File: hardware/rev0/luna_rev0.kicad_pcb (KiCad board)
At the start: 4 copper layers, 48.9 x 50 mm, 132 parts, among them IC1 ECP5-BGA256, J1 USB_B_Micro, J2 USB_B_Micro, J3 USB_A, J4 USB_B_Micro, J5 Conn_ARM_JTAG_SWD_10, J6 Conn_ARM_JTAG_SWD_10, J7 Conn_02x02_Counter_Clockwise, J8 Conn_Coaxial, J9 Conn_Coaxial, SW1 BTN_RECOVERY, SW2 BTN_DFU, SW3 BTN_RESET, U1 AP22814-SOT, U10 S27KS0641, U11 USB3343, U12 AP22814-SOT, U2 MIC5504-1.8YM5, U3 MIC5219-3.3YM5, U4 TCR2EF11, U5 MIC5504-2.5YM5, U6 ATSAMD21G18A-AUT, U7 W25Q32JVSS, U8 USB3343, U9 USB3343, Y1 DSC60xx

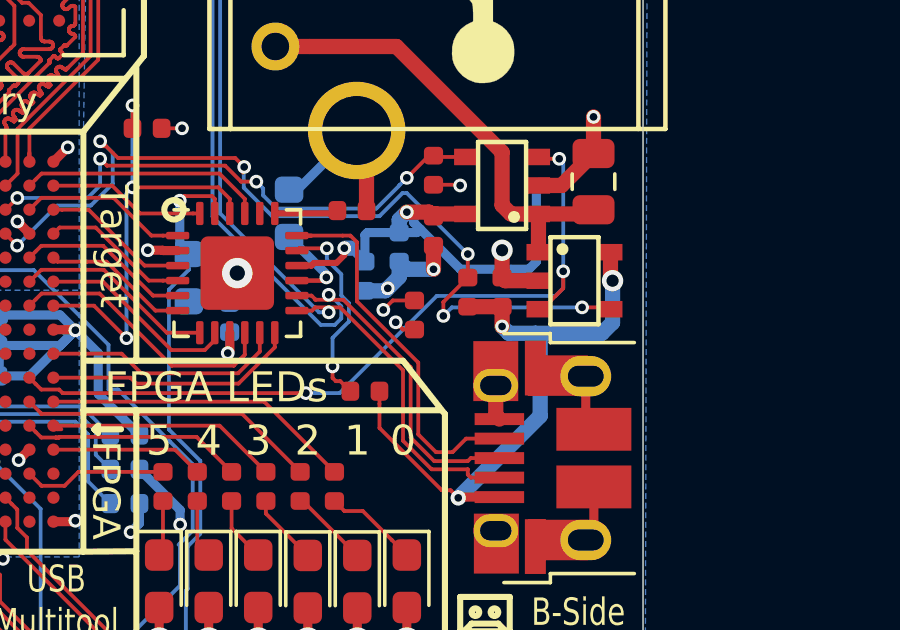
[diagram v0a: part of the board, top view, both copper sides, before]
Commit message: hardware: correct R3 footprint
fix #11
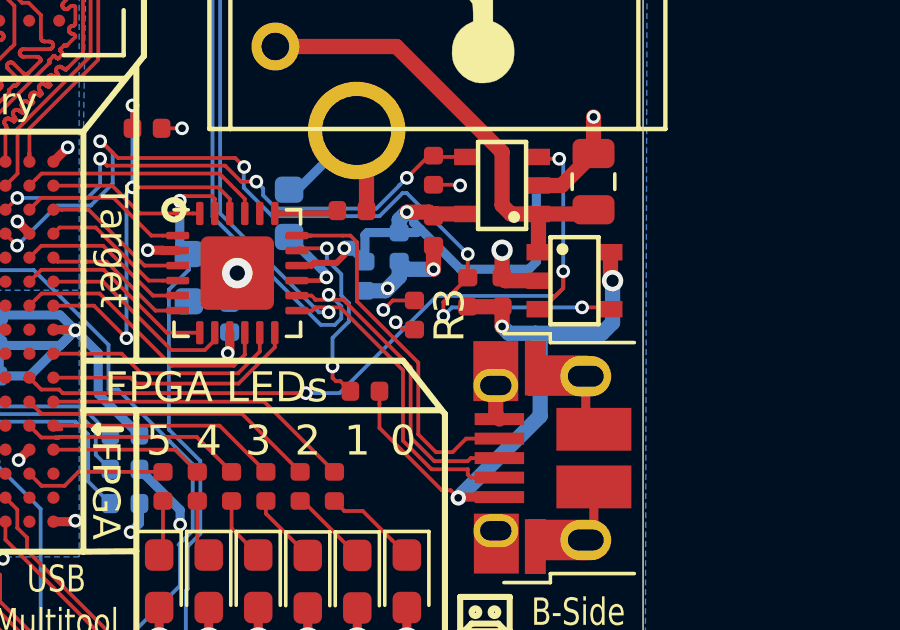
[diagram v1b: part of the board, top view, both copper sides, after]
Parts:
- R12, R13, R14: value 10k -> 10K
- R17, R19, R21: value 20k -> 20K
- R3: footprint Capacitor_SMD:C_0402_1005Metric -> Resistor_SMD:R_0402_1005Metric
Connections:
- U4 pad 4: +1V1 -> Net-(U4-Pad4)
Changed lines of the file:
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@@
-(kicad_pcb (version 20171130) (host pcbnew "(5.1.2-1)-1")
+(kicad_pcb (version 20171130) (host pcbnew 5.1.5)
   (general
     (thickness 1.6)
@@
     (zones 0)
     (modules 132)
-    (nets 284)
+    (nets 285)
   )
   (page A4)
@@
     (pad_to_mask_clearance 0.127)
     (aux_axis_origin 0 0)
-    (visible_elements FEF1BEDF)
+    (visible_elements FEF9BEDF)
     (pcbplotparams
       (layerselection 0x010fc_ffffffff)
@@
   (net 282 /DEBUG_SPI_CS)
   (net 283 "Net-(IC1-PadP12)")
+  (net 284 "Net-(U4-Pad4)")
   (net_class Default "This is the default net class."
     (clearance 0.127)
@@
     (add_net "Net-(U11-Pad20)")
     (add_net "Net-(U2-Pad4)")
+    (add_net "Net-(U4-Pad4)")
     (add_net "Net-(U5-Pad4)")
     (add_net "Net-(U6-Pad32)")
@@
     (add_net "Net-(U9-Pad20)")
   )
+  (module Resistor_SMD:R_0402_1005Metric (layer F.Cu)
+    (at 133.35 88.011 270)
+    (descr "Resistor SMD 0402 (1005 Metric), square (rectangular) end terminal, IPC_7351 nominal, (Body size source: http://www.tortai-tech.com/upload/download/2011102023233369053.pdf), generated with kicad-footprint-generator")
+    (tags resistor)
+    (attr smd)
+    (fp_text reference R3 (at 0 -1.17 90) (layer F.SilkS)
+      (effects (font (size 1 1) (thickness 0.15)))
+    )
+    (fp_text value 10K (at 0 1.17 90) (layer F.Fab)
+      (effects (font (size 1 1) (thickness 0.15)))
+    )
+    (fp_text user %R (at 0 0 90) (layer F.Fab)
+      (effects (font (size 0.25 0.25) (thickness 0.04)))
+    )
+    (fp_line (start 0.93 0.47) (end -0.93 0.47) (layer F.CrtYd) (width 0.05))
+    (fp_line (start 0.93 -0.47) (end 0.93 0.47) (layer F.CrtYd) (width 0.05))
+    (fp_line (start -0.93 -0.47) (end 0.93 -0.47) (layer F.CrtYd) (width 0.05))
+    (fp_line (start -0.93 0.47) (end -0.93 -0.47) (layer F.CrtYd) (width 0.05))
+    (fp_line (start 0.5 0.25) (end -0.5 0.25) (layer F.Fab) (width 0.1))
+    (fp_line (start 0.5 -0.25) (end 0.5 0.25) (layer F.Fab) (width 0.1))
+    (fp_line (start -0.5 -0.25) (end 0.5 -0.25) (layer F.Fab) (width 0.1))
+    (fp_line (start -0.5 0.25) (end -0.5 -0.25) (layer F.Fab) (width 0.1))
+    (pad 2 smd roundrect (at 0.485 0 270) (size 0.59 0.64) (layers F.Cu F.Paste F.Mask) (roundrect_rratio 0.25)
+      (net 36 /TARGET_FAULT))
+    (pad 1 smd roundrect (at -0.485 0 270) (size 0.59 0.64) (layers F.Cu F.Paste F.Mask) (roundrect_rratio 0.25)
+      (net 1 +3V3))
+    (model ${KISYS3DMOD}/Resistor_SMD.3dshapes/R_0402_1005Metric.wrl
+      (at (xyz 0 0 0))
+      (scale (xyz 1 1 1))
+      (rotate (xyz 0 0 0))
+    )
+  )
   (module TestPoint:TestPoint_Pad_D1.0mm (layer B.Cu)
     (at 105.41 76.835)
@@
     )
   )
-  (module Capacitor_SMD:C_0402_1005Metric (layer F.Cu)
-    (at 133.35 88.011 270)
-    (descr "Capacitor SMD 0402 (1005 Metric), square (rectangular) end terminal, IPC_7351 nominal, (Body size source: http://www.tortai-tech.com/upload/download/2011102023233369053.pdf), generated with kicad-footprint-generator")
-    (tags capacitor)
-    (attr smd)
-    (fp_text reference R3 (at 0 -1.17 90) (layer F.SilkS) hide
-      (effects (font (size 1 1) (thickness 0.15)))
-    )
-    (fp_text value 10K (at 0 1.17 90) (layer F.Fab)
-      (effects (font (size 1 1) (thickness 0.15)))
-    )
-    (fp_text user %R (at 0 0 90) (layer F.Fab)
-      (effects (font (size 0.25 0.25) (thickness 0.04)))
-    )
-    (fp_line (start 0.93 0.47) (end -0.93 0.47) (layer F.CrtYd) (width 0.05))
-    (fp_line (start 0.93 -0.47) (end 0.93 0.47) (layer F.CrtYd) (width 0.05))
-    (fp_line (start -0.93 -0.47) (end 0.93 -0.47) (layer F.CrtYd) (width 0.05))
-    (fp_line (start -0.93 0.47) (end -0.93 -0.47) (layer F.CrtYd) (width 0.05))
-    (fp_line (start 0.5 0.25) (end -0.5 0.25) (layer F.Fab) (width 0.1))
-    (fp_line (start 0.5 -0.25) (end 0.5 0.25) (layer F.Fab) (width 0.1))
-    (fp_line (start -0.5 -0.25) (end 0.5 -0.25) (layer F.Fab) (width 0.1))
-    (fp_line (start -0.5 0.25) (end -0.5 -0.25) (layer F.Fab) (width 0.1))
-    (pad 2 smd roundrect (at 0.485 0 270) (size 0.59 0.64) (layers F.Cu F.Paste F.Mask) (roundrect_rratio 0.25)
-      (net 36 /TARGET_FAULT))
-    (pad 1 smd roundrect (at -0.485 0 270) (size 0.59 0.64) (layers F.Cu F.Paste F.Mask) (roundrect_rratio 0.25)
-      (net 1 +3V3))
-    (model ${KISYS3DMOD}/Capacitor_SMD.3dshapes/C_0402_1005Metric.wrl
-      (at (xyz 0 0 0))
-      (scale (xyz 1 1 1))
-      (rotate (xyz 0 0 0))
-    )
-  )
   (module Capacitor_SMD:C_0805_2012Metric (layer F.Cu)
     (at 139.319 83.566 270)
@@
       (effects (font (size 1 1) (thickness 0.15)) (justify mirror))
     )
-    (fp_text value 10k (at 0 -1.17) (layer B.Fab)
+    (fp_text value 10K (at 0 -1.17) (layer B.Fab)
       (effects (font (size 1 1) (thickness 0.15)) (justify mirror))
     )
@@
       (effects (font (size 1 1) (thickness 0.15)) (justify mirror))
     )
-    (fp_text value 10k (at 0 -1.17) (layer B.Fab)
+    (fp_text value 10K (at 0 -1.17) (layer B.Fab)
       (effects (font (size 1 1) (thickness 0.15)) (justify mirror))
     )
@@
       (effects (font (size 1 1) (thickness 0.15)) (justify mirror))
     )
-    (fp_text value 10k (at 0 -1.17) (layer B.Fab)
+    (fp_text value 10K (at 0 -1.17) (layer B.Fab)
       (effects (font (size 1 1) (thickness 0.15)) (justify mirror))
     )
@@
       (effects (font (size 1 1) (thickness 0.15)))
     )
-    (fp_text value 20k (at 0 1.17 90) (layer F.Fab)
+    (fp_text value 20K (at 0 1.17 90) (layer F.Fab)
       (effects (font (size 1 1) (thickness 0.15)))
     )
@@
       (effects (font (size 1 1) (thickness 0.15)))
     )
-    (fp_text value 20k (at 0 1.17) (layer F.Fab)
+    (fp_text value 20K (at 0 1.17) (layer F.Fab)
       (effects (font (size 1 1) (thickness 0.15)))
     )
@@
       (effects (font (size 1 1) (thickness 0.15)))
     )
-    (fp_text value 20k (at 0 1.17) (layer F.Fab)
+    (fp_text value 20K (at 0 1.17) (layer F.Fab)
       (effects (font (size 1 1) (thickness 0.15)))
     )
@@
       (net 2 GND))
     (pad 4 smd rect (at 0.7 0.5) (size 0.45 0.3) (layers F.Cu F.Paste F.Mask)
-      (net 6 +1V1))
+      (net 284 "Net-(U4-Pad4)"))
     (model ${KISYS3DMOD}/Package_TO_SOT_SMD.3dshapes/SOT-553.wrl
       (at (xyz 0 0 0))

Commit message: hardware: update capacitors in schematic
Add parts that were in layout but were missing from schematic.
Update schematic to better represent r0.2 as manufactured.
fix #10
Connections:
- U4 pad 4: Net-(U4-Pad4) -> +1V1
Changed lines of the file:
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@@
     (zones 0)
     (modules 132)
-    (nets 285)
+    (nets 284)
   )
   (page A4)
@@
   (net 282 /DEBUG_SPI_CS)
   (net 283 "Net-(IC1-PadP12)")
-  (net 284 "Net-(U4-Pad4)")
   (net_class Default "This is the default net class."
     (clearance 0.127)
@@
     (add_net "Net-(U11-Pad20)")
     (add_net "Net-(U2-Pad4)")
-    (add_net "Net-(U4-Pad4)")
     (add_net "Net-(U5-Pad4)")
     (add_net "Net-(U6-Pad32)")
@@
       (net 2 GND))
     (pad 4 smd rect (at 0.7 0.5) (size 0.45 0.3) (layers F.Cu F.Paste F.Mask)
-      (net 284 "Net-(U4-Pad4)"))
+      (net 6 +1V1))
     (model ${KISYS3DMOD}/Package_TO_SOT_SMD.3dshapes/SOT-553.wrl
       (at (xyz 0 0 0))

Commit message: hardware: Change U4 to match part number
Update value and symbol name from TCR2EF11 to TCR2EE11.
fix #12
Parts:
- U4: value TCR2EF11 -> TCR2EE11
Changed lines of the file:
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@@
       (effects (font (size 1 1) (thickness 0.15)))
     )
-    (fp_text value TCR2EF11 (at 0 1.75) (layer F.Fab)
+    (fp_text value TCR2EE11 (at 0 1.75) (layer F.Fab)
       (effects (font (size 1 1) (thickness 0.15)))
     )
